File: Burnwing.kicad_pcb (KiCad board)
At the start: 4 copper layers, 50.8 x 22.9 mm, 42 parts, among them J1 USB Type C, J2 Conn_01x06_MountingPin, Q2 AONR21307, U1 HUSB238, U2 BTS7030-2EPA

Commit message: google drive upload
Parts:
- removed the REF** at (88.1, 99.5)
- added 12V1: SOLDERJUMPER, Library:SOLDERJUMPER_ARROW_NOPASTE, F.Cu at (86.1, 99.8)
- added 1A1: SOLDERJUMPERCLOSED, Library:SOLDERJUMPER_CLOSEDWIRE, F.Cu at (88.4, 99.8)
- added 2A1: SOLDERJUMPER, Library:SOLDERJUMPER_ARROW_NOPASTE, F.Cu at (90.7, 99.7)
- added 5V1: SOLDERJUMPERCLOSED, Library:SOLDERJUMPER_CLOSEDWIRE, F.Cu at (83.8, 99.8)
- added R18: 14K, Library:R_0603_1608Metric_Pad0.98x0.95mm_HandSolder, F.Cu at (88.7, 96.3)
- Burn1, Burn2: footprint Library:KEY-SMD_4P-L6.0-W6.0-P4.50-LS9.5-BR -> EasyEDA:KEY-SMD_4P-L6.0-W6.0-P4.50-LS9.5-BR
- U2: footprint Library:PG-TSDSO-14_L4.9-W3.9-P0.65-LS6.0-BL-EP -> EasyEDA:PG-TSDSO-14_L4.9-W3.9-P0.65-LS6.0-BL-EP
- moved R9 15.3 mm to (93.9, 88.6), turned to 180 degrees
- moved R16 8.50 mm to (108.5, 88.5)
- moved R15 3.82 mm to (93.9, 86.8)
- moved D2 3.57 mm to (101.8, 91.6), turned to 90 degrees
- moved D1 3.18 mm to (95.2, 91.6), turned to 90 degrees
- moved R7 2.97 mm to (87.0, 96.3), turned to 90 degrees
- moved C1 2.55 mm to (88.8, 90.0)
- moved R6 2.29 mm to (108.5, 90.2), turned to 180 degrees
- moved .space 1.76 mm to (111.2, 101.3)
- moved R8 1.42 mm to (85.2, 96.3), turned to 90 degrees
- moved U1 0.75 mm to (88.7, 92.8)
- moved U2 0.59 mm to (108.0, 95.2)
- moved R1 0.53 mm to (115.3, 91.5)
- moved REF** 0.53 mm to (116.3, 91.5)
- moved R2 0.50 mm to (121.5, 91.5)
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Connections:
- R7 pad 1: GND -> Net-(2A1-Pad2)
- R8 pad 1: GND -> Net-(12V1-Pad1)
- REF** pad 1: GND -> VDC (x2)
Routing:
- net BURN_CTRL_1: track 11.3 -> 24.8 mm, vias 0 -> 2
- net BURN_CTRL_2: track 11.8 -> 18.4 mm, vias 0 -> 2
- net Net-(D1-A): track 1.37 -> 7.20 mm
- net Net-(U1-VIN): track 5.70 -> 0.00 mm
- net Net-(2A1-Pad2): track 0.00 -> 5.47 mm
- net Net-(D2-A): track 1.64 -> 6.71 mm
- net Net-(U1-VSET): track 8.16 -> 12.1 mm
- net /D+: track 9.77 -> 6.31 mm
- net Net-(U1-ISET): track 8.39 -> 11.7 mm, vias 0 -> 2
- net Net-(12V1-Pad1): track 0.00 -> 2.16 mm
- net Net-(R1-Pad2): track 9.62 -> 7.94 mm
- net /D-: track 7.66 -> 6.60 mm, vias 2 -> 0
- net /CC2: track 3.00 -> 3.74 mm
- net /CC1: track 5.22 -> 5.95 mm
- net Net-(Q2-G): track 3.20 -> 2.68 mm
- added copper zone on B.Cu, net (none)
- added copper zone on F.Cu, net (none)
- removed copper zone on B.Cu, net GND
- removed copper zone on F.Cu, net GND
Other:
- board text removed: "12V"
- board text removed: "1A"
- board text removed: "2A"
- board text removed: "5V"

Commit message: Separated Version
-Added dipswitch for Vset and Iset
-Added tentative microcontroller and jumper pins
-Separated flight and not flight modes
-Removed SCL/SDA
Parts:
- removed 12V1, 2A1: SOLDERJUMPER, Library:SOLDERJUMPER_ARROW_NOPASTE
- removed 1A1, 5V1: SOLDERJUMPERCLOSED, Library:SOLDERJUMPER_CLOSEDWIRE
- removed R18: 14K, Library:R_0603_1608Metric_Pad0.98x0.95mm_HandSolder
- added D4: 1N4148WT, Diode_SMD:D_SOD-523, F.Cu at (96.0, 89.6)
- added D5: 1N4148WT, Diode_SMD:D_SOD-523, F.Cu at (109.8, 89.0)
- added J4: Conn_01x04_Pin, Connector_PinSocket_1.00mm:PinSocket_1x04_P1.00mm_Vertical, F.Cu at (111.2, 81.2)
- added JP1: Jumper_3_Bridged12, Connector_PinSocket_1.00mm:PinSocket_1x03_P1.00mm_Vertical, F.Cu at (91.7, 86.3)
- added JP2: Jumper_3_Bridged12, Connector_PinSocket_1.00mm:PinSocket_1x03_P1.00mm_Vertical, F.Cu at (105.5, 88.7)
- added R10: R, Library:R_0603_1608Metric_Pad0.98x0.95mm_HandSolder, F.Cu at (110.7, 85.9)
- added R19: R, Library:R_0603_1608Metric_Pad0.98x0.95mm_HandSolder, F.Cu at (112.2, 85.9)
- added SW1: SW_DIP_x02, Library:2_Dipswitch, F.Cu at (86.0, 99.6)
- moved R6 9.93 mm to (98.6, 90.2), turned to 0 degrees
- moved R16 6.24 mm to (102.3, 89.2)
- moved C2 6.10 mm to (87.9, 82.7), turned to -90 degrees
- moved R9 5.64 mm to (94.0, 83.0), turned to -90 degrees
- moved R8 4.25 mm to (89.4, 96.4)
- moved C4 2.24 mm to (92.0, 82.7), turned to -90 degrees
- moved R15 2.06 mm to (93.4, 88.8)
- moved C3 1.98 mm to (90.0, 82.7), turned to -90 degrees
- moved Q2 1.81 mm to (85.0, 83.2)
- moved R4 1.17 mm to (89.5, 87.2), turned to 90 degrees
- moved R7 1.13 mm to (86.2, 95.4), turned to 0 degrees
- moved D1 0.86 mm to (94.3, 91.7)
- moved C1 0.78 mm to (88.0, 90.0)
- moved D2 0.76 mm to (101.0, 91.7)
- moved Burn1 0.75 mm to (94.3, 96.7)
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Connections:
- Burn1 pad 3: BURN_CTRL_1 -> Net-(Burn1-C)
- Burn1 pad 4: BURN_CTRL_1 -> Net-(Burn1-C)
- Burn2 pad 3: BURN_CTRL_2 -> Net-(Burn2-C)
- Burn2 pad 4: BURN_CTRL_2 -> Net-(Burn2-C)
- R15 pad 1: BURN_CTRL_1 -> Net-(Burn1-C)
- R16 pad 1: BURN_CTRL_2 -> Net-(Burn2-C)
- R6 pad 1: BURN_CTRL_2 -> GND
- R6 pad 2: GND -> /GATE2
- R7 pad 1: Net-(2A1-Pad2) -> GND
- R8 pad 1: Net-(12V1-Pad1) -> GND
- R9 pad 1: BURN_CTRL_1 -> GND
- R9 pad 2: GND -> /GATE1
- U1 pad 6: /SDA -> unconnected-(U1-SDA-Pad6)
- U1 pad 7: /SCL -> unconnected-(U1-SCL-Pad7)
- U2 pad 2: BURN_CTRL_1 -> /GATE1
- U2 pad 6: BURN_CTRL_2 -> /GATE2
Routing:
- net /GATE1: track 0.00 -> 21.5 mm, vias 0 -> 3
- net Net-(D4-A): track 0.00 -> 15.5 mm, vias 0 -> 2
- net /GATE2: track 0.00 -> 13.7 mm, vias 0 -> 2
- net Net-(Burn2-C): track 0.00 -> 13.0 mm, vias 0 -> 2
- net BURN_CTRL_2: track 18.4 -> 5.60 mm, vias 2 -> 0
- net BURN_CTRL_1: track 24.8 -> 13.3 mm
- net Net-(Burn1-C): track 0.00 -> 7.60 mm
- net GND: track 2.87 -> 9.53 mm, vias 0 -> 23
- net Net-(2A1-Pad2): track 5.47 -> 0.00 mm
- net Net-(D2-A): track 6.71 -> 1.74 mm
- net Net-(U1-VSET): track 12.1 -> 7.29 mm
- net Net-(D1-A): track 7.20 -> 2.73 mm
- net MICRO_BURN_1: track 0.00 -> 4.43 mm
- net Net-(U1-VIN): track 0.00 -> 4.30 mm
- net MICRO_BURN_2: track 0.00 -> 4.20 mm
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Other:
- board text added: "12V"
- board text added: "1A"
- board text added: "2A"
- board text added: "5V"

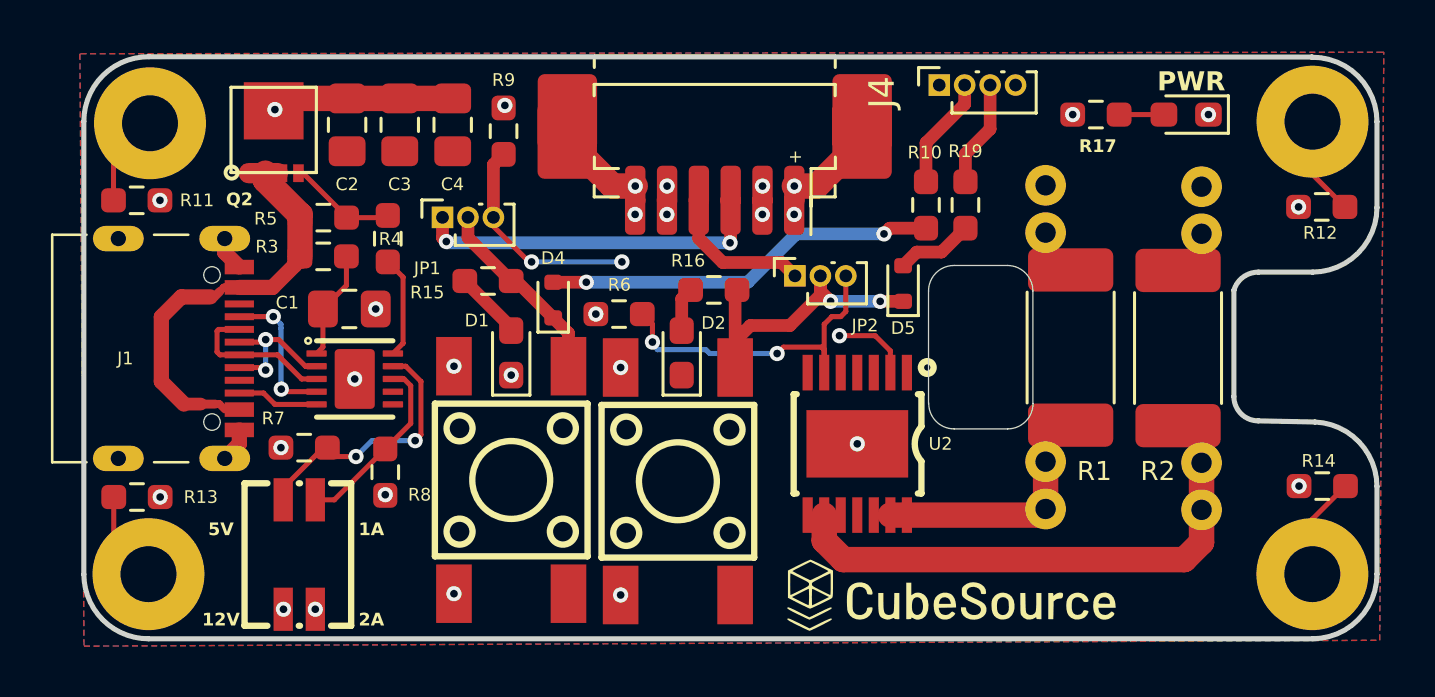
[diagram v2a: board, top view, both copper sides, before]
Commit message: Fixed Vias Issues
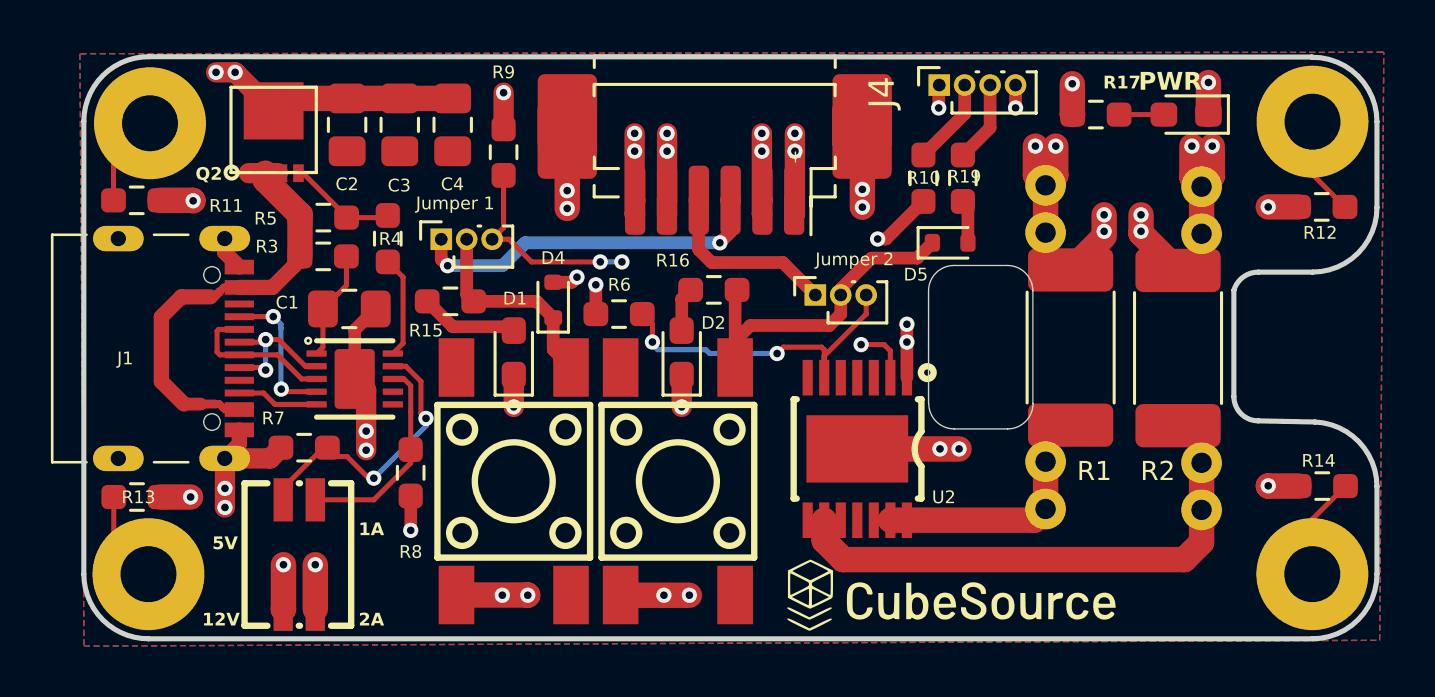
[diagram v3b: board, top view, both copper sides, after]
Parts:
- Jumper 1: renamed from JP1
- Jumper 2: renamed from JP2
- moved D5 2.45 mm to (111.6, 87.3), turned to 0 degrees
- moved R15 1.68 mm to (92.0, 89.7)
- moved Jumper 2 1.10 mm to (106.3, 89.4)
- moved R10 1.05 mm to (110.5, 84.8)
- moved R19 1.05 mm to (112.1, 84.8)
- moved R8 1.00 mm to (90.4, 96.4)
- moved Jumper 1 0.86 mm to (91.6, 87.2)
- moved R9 0.82 mm to (94.0, 83.8)
- moved U2 0.20 mm to (108.0, 95.5)
- moved Burn1 0.11 mm to (94.5, 96.7)
- moved D1 0.10 mm to (94.5, 91.7)
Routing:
- net GND: track 9.53 -> 54.9 mm, vias 23 -> 32
- net VDC: track 8.42 -> 33.5 mm, vias 12 -> 18
- net Net-(D4-A): track 15.5 -> 17.1 mm
- net BURN_CTRL_2: track 5.60 -> 6.97 mm
- net Net-(D5-A): track 3.06 -> 1.71 mm
- net Net-(D1-A): track 2.73 -> 4.00 mm
- net Net-(Burn2-C): track 13.0 -> 14.1 mm, vias 2 -> 0
- net MICRO_BURN_1: track 4.43 -> 3.42 mm
- net MICRO_BURN_2: track 4.20 -> 3.19 mm
- net Net-(U1-VSET): track 7.29 -> 8.20 mm
- net Net-(U1-ISET): track 10.5 -> 11.3 mm
- net Net-(Burn1-C): track 7.60 -> 8.19 mm
- net BURN_CTRL_1: track 13.3 -> 13.8 mm

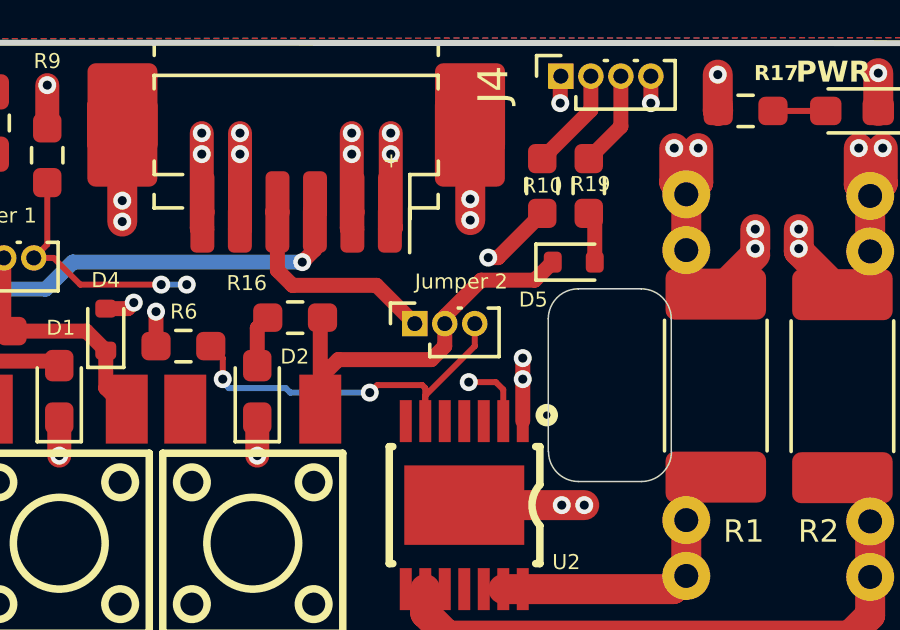
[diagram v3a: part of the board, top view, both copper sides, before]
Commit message: QR Code Shifting
Moved Jumper 2, QR Code, CubeSource link, and Burnwing Rev2
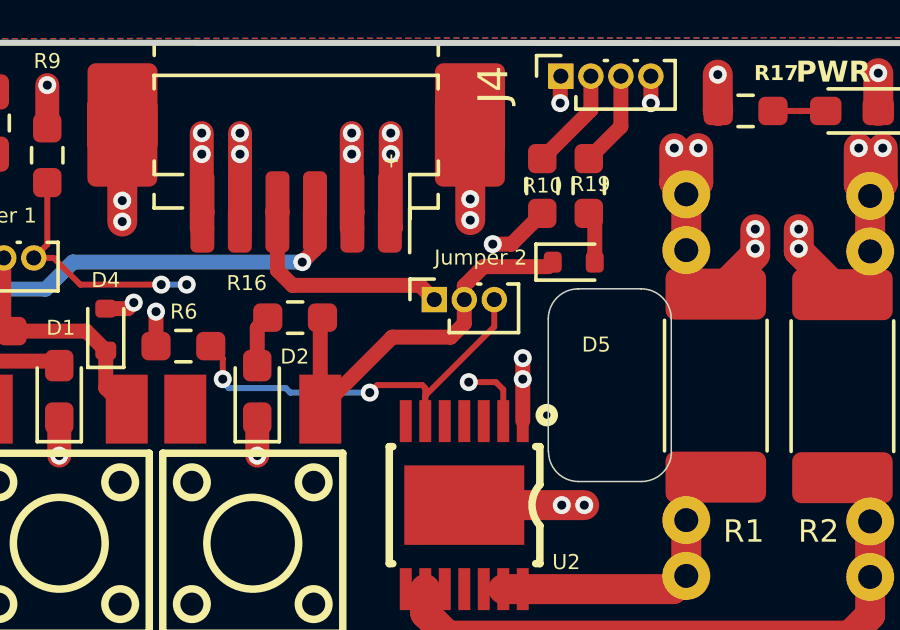
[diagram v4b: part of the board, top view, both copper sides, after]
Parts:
- moved G*** 2.68 mm to (100.3, 91.1)
- moved .space 2.48 mm to (102.5, 99.6)
- moved Jumper 2 1.03 mm to (107.0, 88.6)
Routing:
- net /GATE2: track 13.2 -> 14.3 mm
- net Net-(Burn2-C): track 14.1 -> 14.6 mm

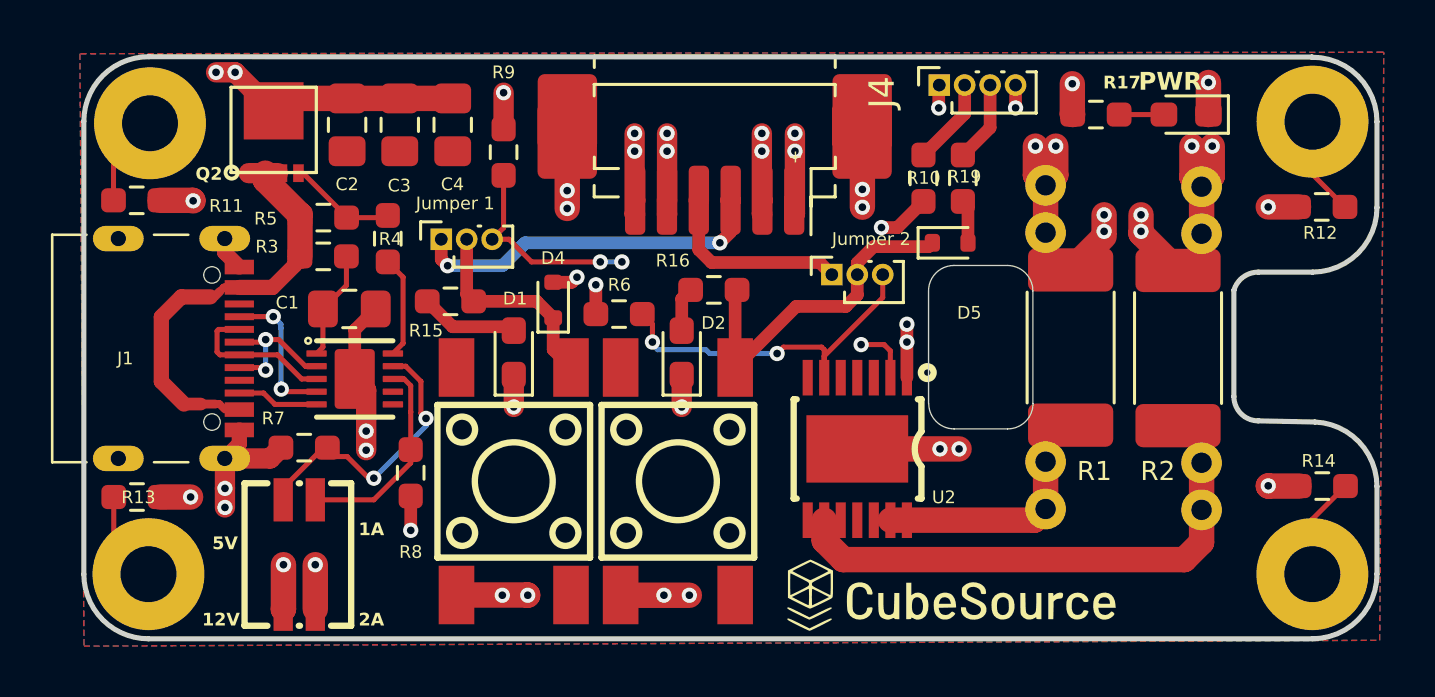
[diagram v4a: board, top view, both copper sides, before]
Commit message: fixing traces/vias
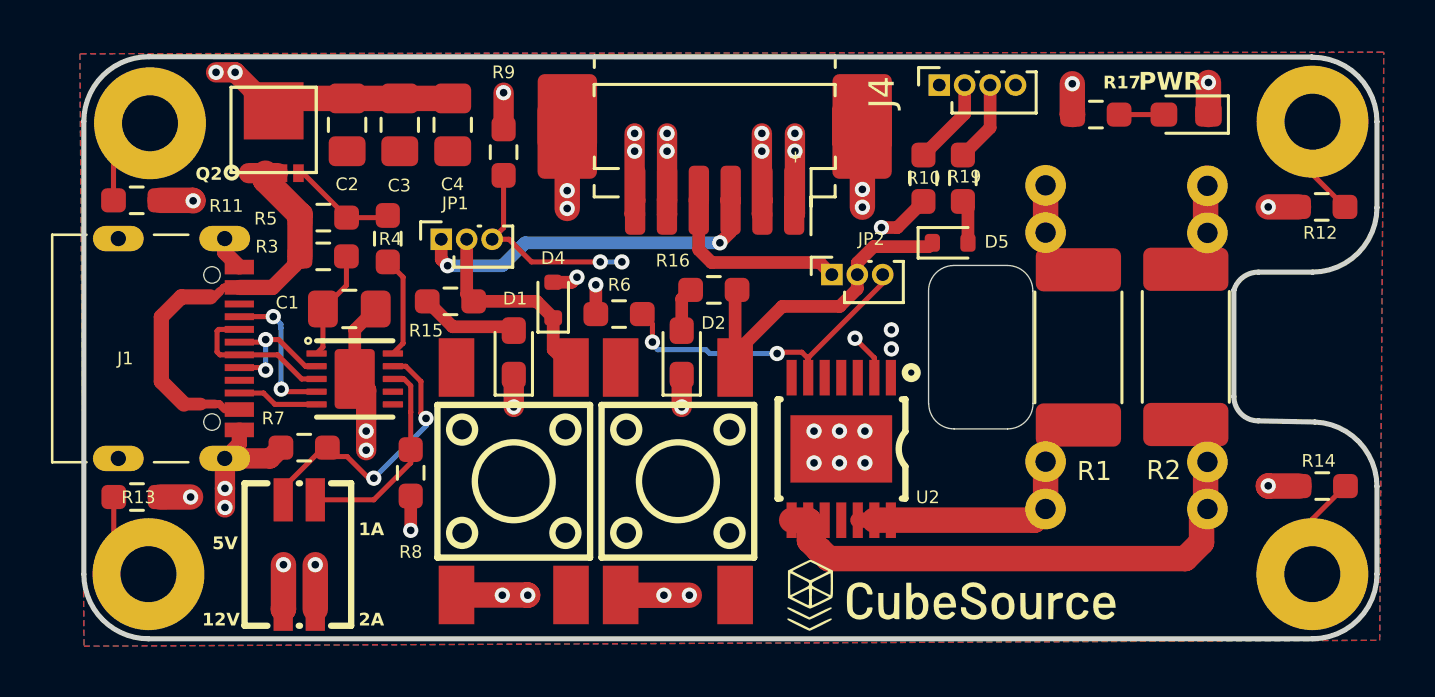
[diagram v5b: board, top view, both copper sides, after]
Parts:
- JP1: renamed from Jumper 1
- JP2: renamed from Jumper 2
- moved U2 0.63 mm to (107.3, 95.5)
- moved REF** 0.31 mm to (120.9, 91.4)
- moved REF** 0.31 mm to (116.6, 91.5)
- moved R2 0.23 mm to (121.7, 91.5)
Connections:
- REF** pad 1: VDC -> GND (x2)
- REF** pad 2: Net-(Q1-D2-Pad5) -> Net-(R2-Pad2)
- REF** pad 2: Net-(Q1-D1-Pad7) -> Net-(R1-Pad2)
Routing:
- net VDC: track 33.5 -> 23.3 mm, vias 18 -> 17
- net GND: track 54.9 -> 44.9 mm, vias 32 -> 26
- net Net-(R1-Pad2): track 8.03 -> 11.1 mm
- net Net-(R2-Pad2): track 19.3 -> 22.3 mm
- net /GATE1: track 21.0 -> 20.2 mm
- added copper zone on B.Cu, net GND
- added copper zone on F.Cu, net GND
- removed copper zone on B.Cu, net (none)
- removed copper zone on F.Cu, net (none)

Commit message: Fixed VDC traces
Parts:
- moved .space 0.11 mm to (111.2, 101.4)
- turned C2 to 90 degrees
- turned C3 to 90 degrees
- turned C4 to 90 degrees
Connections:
- Burn1 pad 3: Net-(Burn1-C) -> (no net)
- Burn2 pad 3: Net-(Burn2-C) -> (no net)
- C2 pad 2: Net-(C2-Pad2) -> GND
- C3 pad 2: Net-(C2-Pad2) -> GND
- C4 pad 2: Net-(C2-Pad2) -> GND
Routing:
- net VDC: track 23.3 -> 27.2 mm, vias 17 -> 18
- net GND: track 44.9 -> 48.3 mm
- net Net-(R2-Pad2): track 22.3 -> 21.0 mm
- net Net-(Burn2-C): track 14.8 -> 13.8 mm
- net Net-(R1-Pad2): track 11.1 -> 10.5 mm
